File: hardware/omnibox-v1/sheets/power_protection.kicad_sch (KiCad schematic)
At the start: 22 parts

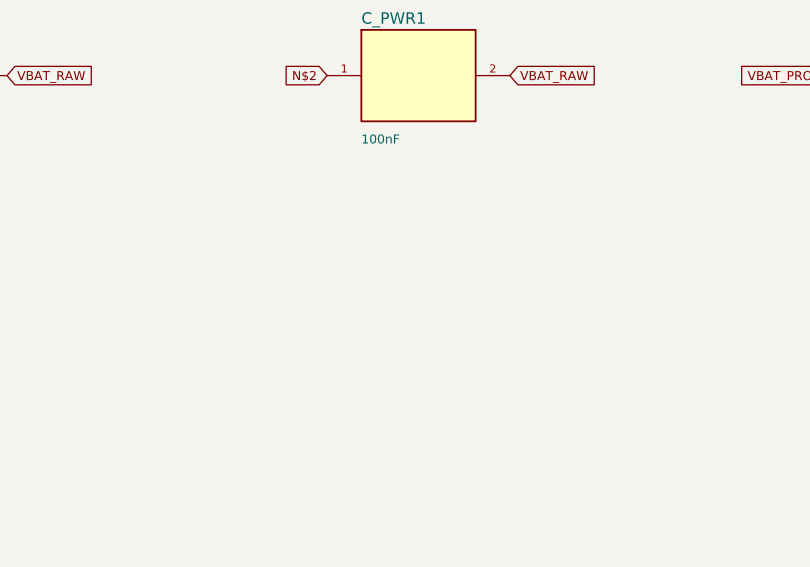
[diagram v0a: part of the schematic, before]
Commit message: fix(hardware): sync omnibox-v1 with the repaired J2534 V1 KiCad project
Replace the schematic and board with the corrected, single-source-of-truth
version from the upstream J2534 V1 project, and consolidate to one project.

- Schematic + board replaced by the repaired versions (schematic<->PCB relinked
  by symbol UUIDs, 296 (path) links; legal reference designators; library
  prefixes restored on all footprints; USB SuperSpeed pins and MCP2518FD pin 15
  removed to match the fitted footprints; split nets merged: KLINE1/J1962_P7,
  J1850_BUS/J1850_BUSN). Internal project name set to omnibox-v1, company OmniBox.
- Corrected symbols (sym-lib/j2534gen, j2534_local) and footprint libraries.
- Design constraints and net classes aligned to the as-built board (min via
  0.4 mm, min drill 0.2 mm, net-class clearance 0.15 mm).
- Custom DRC rules (.kicad_dru) fixed: '=~' -> '==' (KiCad has no regex; '=='
  does wildcard matching), tightened MCP*CAN / J1850_BUS* patterns, VDDA on the
  host side. Isolation barrier verified with 0 violations, 0 DRC errors.
- Removed the duplicate production/local-finish project; regenerated the
  netlist, consolidated BOM, schematic PDF and Gerbers as omnibox-v1-*.
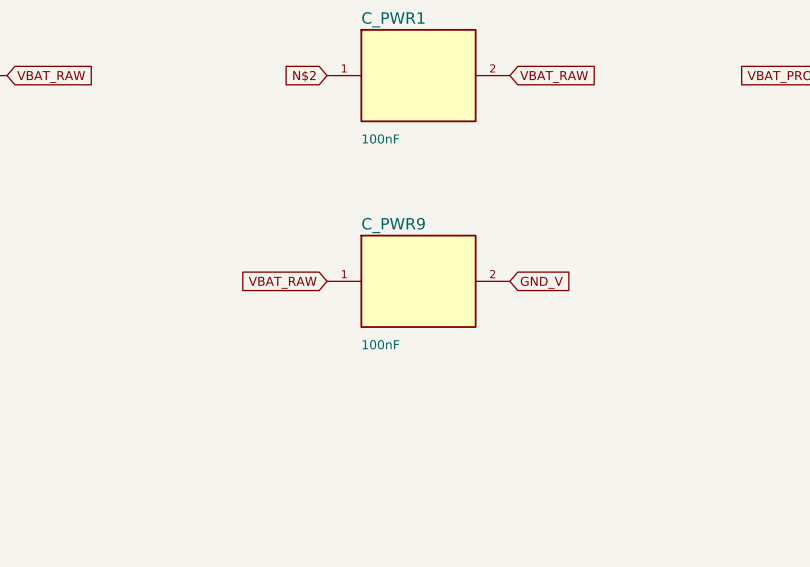
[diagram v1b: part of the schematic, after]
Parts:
- added C_PWR9: 100nF, Capacitor_SMD:C_0603_1608Metric, symbol j2534gen:Device_C
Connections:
- net GND_V: now also C_PWR9.2
- net VBAT_RAW: now also C_PWR9.1
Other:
- company: Interface USB-OBD J2534 -> OmniBox
